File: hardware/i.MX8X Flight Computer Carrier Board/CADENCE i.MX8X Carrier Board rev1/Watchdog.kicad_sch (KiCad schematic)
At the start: 36 parts, among them U7 TLV1704

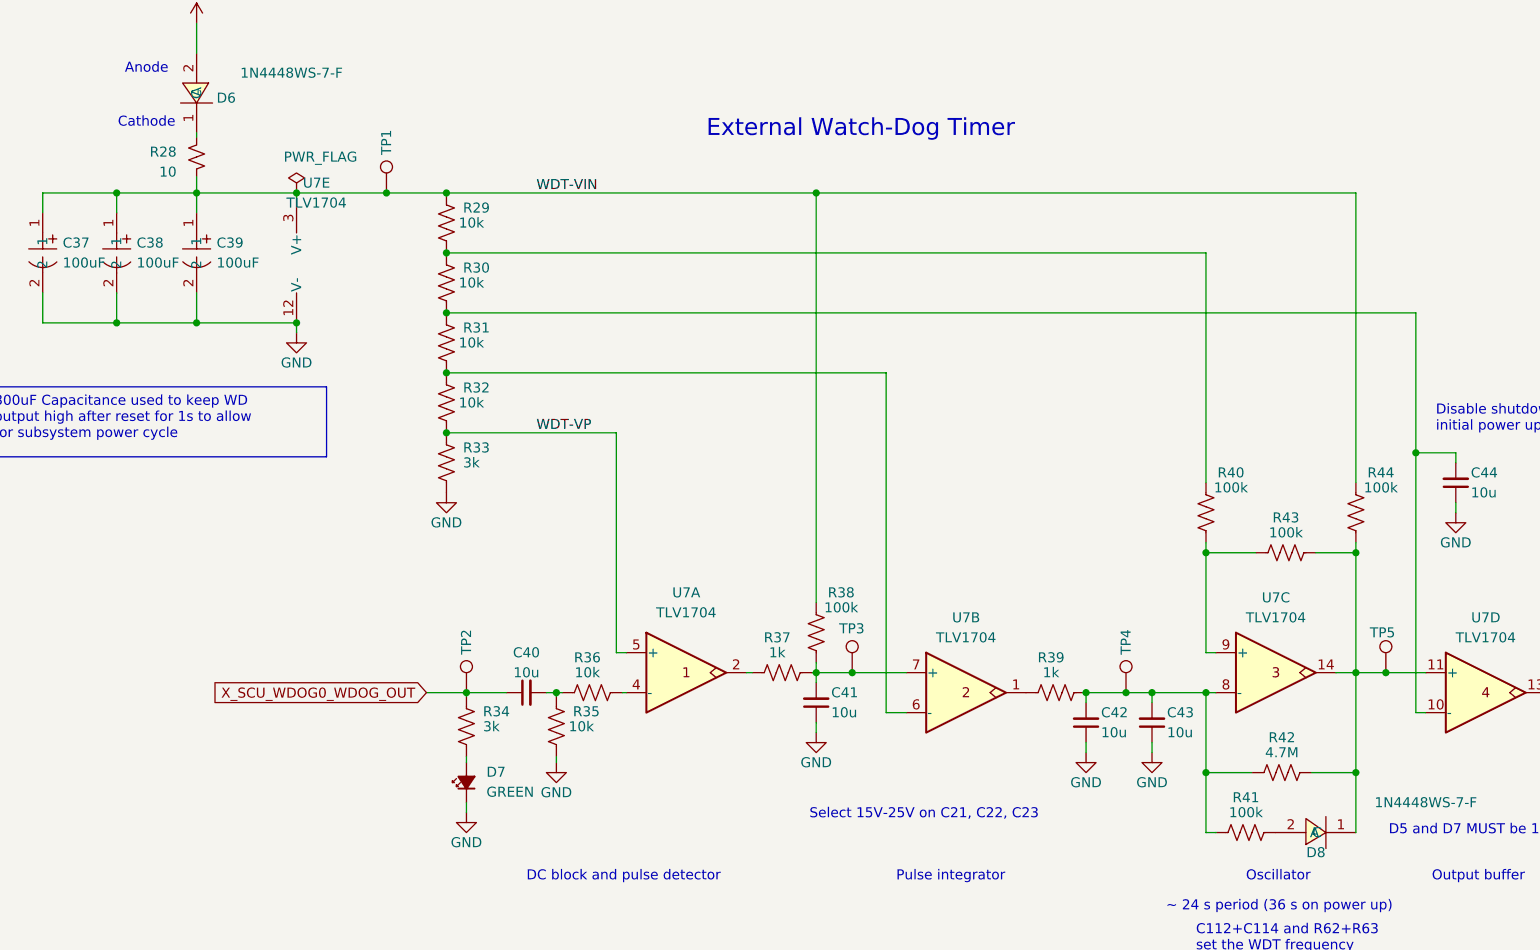
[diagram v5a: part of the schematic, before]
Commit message: Added pin definitions page
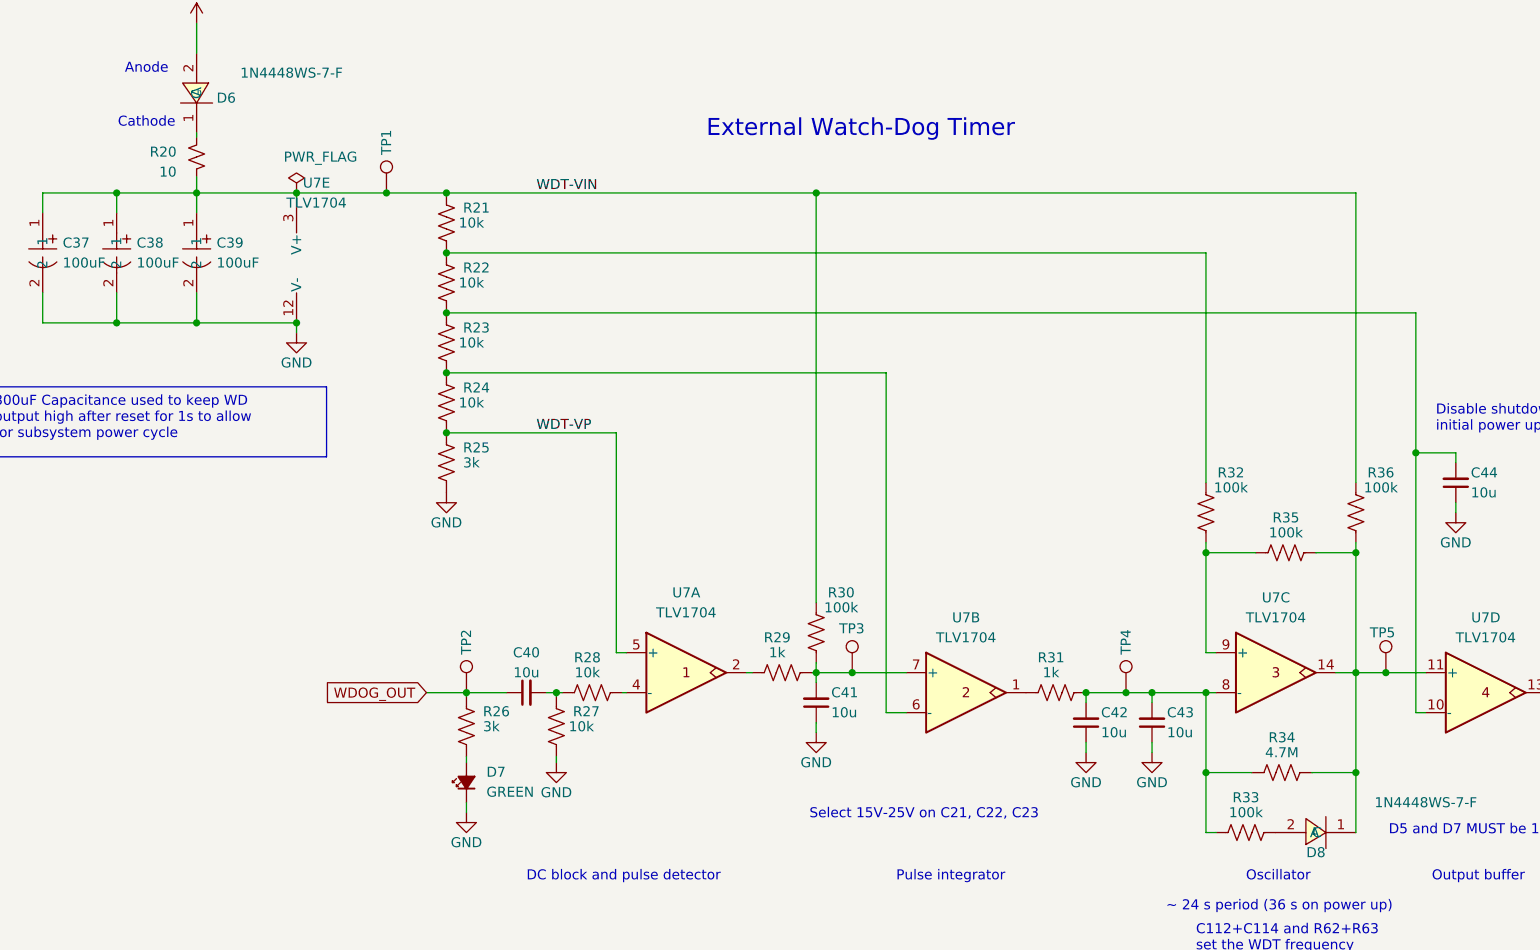
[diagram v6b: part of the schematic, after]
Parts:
- renumbered R28 to R20, R29 to R21, R30 to R22, R31 to R23, R32 to R24, R33 to R25, R34 to R26, R35 to R27, R36 to R28, R37 to R29, R38 to R30, R39 to R31, R40 to R32, R41 to R33, R42 to R34, R43 to R35, R44 to R36
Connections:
- net X_SCU_WDOG0_WDOG_OUT renamed WDOG_OUT
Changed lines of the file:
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@@
 		)
 	)
-	(global_label "X_SCU_WDOG0_WDOG_OUT"
+	(global_label "WDOG_OUT"
 		(shape input)
 		(at 77.47 114.3 180)
@@
 		)
 		(property "Intersheetrefs" "${INTERSHEET_REFS}"
-			(at 50.113 114.3 0)
+			(at 64.5667 114.3 0)
 			(effects
 				(font
@@
 		(on_board yes)
 		(dnp no)
-		(property "Reference" "R34"
+		(property "Reference" "R26"
 			(at 86.36 116.713 0)
 			(effects
@@
 			(project "CADENCE i.MX8X Carrier Board rev1"
 				(path "/de284495-d382-47cb-b528-76e440980d40/59642966-a844-41dc-8ff0-cc80b38f7a57"
-					(reference "R34")
+					(reference "R26")
 					(unit 1)
 				)
@@
 		(on_board yes)
 		(dnp no)
-		(property "Reference" "R36"
+		(property "Reference" "R28"
 			(at 97.917 109.855 90)
 			(effects
@@
 			(project "CADENCE i.MX8X Carrier Board rev1"
 				(path "/de284495-d382-47cb-b528-76e440980d40/59642966-a844-41dc-8ff0-cc80b38f7a57"
-					(reference "R36")
+					(reference "R28")
 					(unit 1)
 				)
@@
 		(on_board yes)
 		(dnp no)
-		(property "Reference" "R43"
+		(property "Reference" "R35"
 			(at 186.69 92.075 90)
 			(effects
@@
 			(project "CADENCE i.MX8X Carrier Board rev1"
 				(path "/de284495-d382-47cb-b528-76e440980d40/59642966-a844-41dc-8ff0-cc80b38f7a57"
-					(reference "R43")
+					(reference "R35")
 					(unit 1)
 				)
@@
 		(on_board yes)
 		(dnp no)
-		(property "Reference" "#PWR042"
+		(property "Reference" "#PWR043"
 			(at 93.98 129.54 0)
 			(effects
@@
 			(project "CADENCE i.MX8X Carrier Board rev1"
 				(path "/de284495-d382-47cb-b528-76e440980d40/59642966-a844-41dc-8ff0-cc80b38f7a57"
-					(reference "#PWR042")
+					(reference "#PWR043")
 					(unit 1)
 				)
@@
 		(on_board yes)
 		(dnp no)
-		(property "Reference" "#PWR041"
+		(property "Reference" "#PWR042"
 			(at 82.55 135.89 0)
 			(effects
@@
 			(project "CADENCE i.MX8X Carrier Board rev1"
 				(path "/de284495-d382-47cb-b528-76e440980d40/59642966-a844-41dc-8ff0-cc80b38f7a57"
-					(reference "#PWR041")
+					(reference "#PWR042")
 					(unit 1)
 				)
@@
 		(on_board yes)
 		(dnp no)
-		(property "Reference" "#PWR045"
+		(property "Reference" "#PWR046"
 			(at 169.672 128.27 0)
 			(effects
@@
 			(project "CADENCE i.MX8X Carrier Board rev1"
 				(path "/de284495-d382-47cb-b528-76e440980d40/59642966-a844-41dc-8ff0-cc80b38f7a57"
-					(reference "#PWR045")
+					(reference "#PWR046")
 					(unit 1)
 				)
@@
 		(on_board yes)
 		(dnp no)
-		(property "Reference" "#PWR040"
+		(property "Reference" "#PWR041"
 			(at 80.01 95.25 0)
 			(effects
@@
 			(project "CADENCE i.MX8X Carrier Board rev1"
 				(path "/de284495-d382-47cb-b528-76e440980d40/59642966-a844-41dc-8ff0-cc80b38f7a57"
-					(reference "#PWR040")
+					(reference "#PWR041")
 					(unit 1)
 				)
@@
 		(on_board yes)
 		(dnp no)
-		(property "Reference" "R30"
+		(property "Reference" "R22"
 			(at 83.82 60.325 0)
 			(effects
@@
 			(project "CADENCE i.MX8X Carrier Board rev1"
 				(path "/de284495-d382-47cb-b528-76e440980d40/59642966-a844-41dc-8ff0-cc80b38f7a57"
-					(reference "R30")
+					(reference "R22")
 					(unit 1)
 				)
@@
 		(on_board yes)
 		(dnp no)
-		(property "Reference" "R33"
+		(property "Reference" "R25"
 			(at 83.82 83.185 0)
 			(effects
@@
 			(project "CADENCE i.MX8X Carrier Board rev1"
 				(path "/de284495-d382-47cb-b528-76e440980d40/59642966-a844-41dc-8ff0-cc80b38f7a57"
-					(reference "R33")
+					(reference "R25")
 					(unit 1)
 				)
@@
 		(on_board yes)
 		(dnp no)
-		(property "Reference" "R39"
+		(property "Reference" "R31"
 			(at 156.845 109.855 90)
 			(effects
@@
 			(project "CADENCE i.MX8X Carrier Board rev1"
 				(path "/de284495-d382-47cb-b528-76e440980d40/59642966-a844-41dc-8ff0-cc80b38f7a57"
-					(reference "R39")
+					(reference "R31")
 					(unit 1)
 				)
@@
 		(on_board yes)
 		(dnp no)
-		(property "Reference" "R31"
+		(property "Reference" "R23"
 			(at 83.82 67.945 0)
 			(effects
@@
 			(project "CADENCE i.MX8X Carrier Board rev1"
 				(path "/de284495-d382-47cb-b528-76e440980d40/59642966-a844-41dc-8ff0-cc80b38f7a57"
-					(reference "R31")
+					(reference "R23")
 					(unit 1)
 				)
@@
 		(on_board yes)
 		(dnp no)
-		(property "Reference" "#PWR043"
+		(property "Reference" "#PWR044"
 			(at 127 125.73 0)
 			(effects
@@
 			(project "CADENCE i.MX8X Carrier Board rev1"
 				(path "/de284495-d382-47cb-b528-76e440980d40/59642966-a844-41dc-8ff0-cc80b38f7a57"
-					(reference "#PWR043")
+					(reference "#PWR044")
 					(unit 1)
 				)
@@
 		(on_board yes)
 		(dnp no)
-		(property "Reference" "R32"
+		(property "Reference" "R24"
 			(at 83.82 75.565 0)
 			(effects
@@
 			(project "CADENCE i.MX8X Carrier Board rev1"
 				(path "/de284495-d382-47cb-b528-76e440980d40/59642966-a844-41dc-8ff0-cc80b38f7a57"
-					(reference "R32")
+					(reference "R24")
 					(unit 1)
 				)
@@
 		(on_board yes)
 		(dnp no)
-		(property "Reference" "#PWR039"
+		(property "Reference" "#PWR040"
 			(at 60.96 74.93 0)
 			(effects
@@
 			(project "CADENCE i.MX8X Carrier Board rev1"
 				(path "/de284495-d382-47cb-b528-76e440980d40/59642966-a844-41dc-8ff0-cc80b38f7a57"
-					(reference "#PWR039")
+					(reference "#PWR040")
 					(unit 1)
 				)
@@
 		(on_board yes)
 		(dnp no)
-		(property "Reference" "#PWR044"
+		(property "Reference" "#PWR045"
 			(at 161.29 128.27 0)
 			(effects
@@
 			(project "CADENCE i.MX8X Carrier Board rev1"
 				(path "/de284495-d382-47cb-b528-76e440980d40/59642966-a844-41dc-8ff0-cc80b38f7a57"
-					(reference "#PWR044")
+					(reference "#PWR045")
 					(unit 1)
 				)
@@
 		(on_board yes)
 		(dnp no)
-		(property "Reference" "R28"
+		(property "Reference" "R20"
 			(at 45.72 45.593 0)
 			(effects
@@
 			(project "CADENCE i.MX8X Carrier Board rev1"
 				(path "/de284495-d382-47cb-b528-76e440980d40/59642966-a844-41dc-8ff0-cc80b38f7a57"
-					(reference "R28")
+					(reference "R20")
 					(unit 1)
 				)
@@
 		(on_board yes)
 		(dnp no)
-		(property "Reference" "R44"
+		(property "Reference" "R36"
 			(at 198.755 86.36 0)
 			(effects
@@
 			(project "CADENCE i.MX8X Carrier Board rev1"
 				(path "/de284495-d382-47cb-b528-76e440980d40/59642966-a844-41dc-8ff0-cc80b38f7a57"
-					(reference "R44")
+					(reference "R36")
 					(unit 1)
 				)
@@
 		(on_board yes)
 		(dnp no)
-		(property "Reference" "R37"
+		(property "Reference" "R29"
 			(at 122.047 107.315 90)
 			(effects
@@
 			(project "CADENCE i.MX8X Carrier Board rev1"
 				(path "/de284495-d382-47cb-b528-76e440980d40/59642966-a844-41dc-8ff0-cc80b38f7a57"
-					(reference "R37")
+					(reference "R29")
 					(unit 1)
 				)
@@
 		(on_board yes)
 		(dnp no)
-		(property "Reference" "R41"
+		(property "Reference" "R33"
 			(at 181.61 127.635 90)
 			(effects
@@
 			(project "CADENCE i.MX8X Carrier Board rev1"
 				(path "/de284495-d382-47cb-b528-76e440980d40/59642966-a844-41dc-8ff0-cc80b38f7a57"
-					(reference "R41")
+					(reference "R33")
 					(unit 1)
 				)
@@
 		(dnp no)
 		(fields_autoplaced yes)
-		(property "Reference" "#PWR038"
+		(property "Reference" "#PWR039"
 			(at 48.26 33.02 0)
 			(effects
@@
 			(project "CADENCE i.MX8X Carrier Board rev1"
 				(path "/de284495-d382-47cb-b528-76e440980d40/59642966-a844-41dc-8ff0-cc80b38f7a57"
-					(reference "#PWR038")
+					(reference "#PWR039")
 					(unit 1)
 				)
@@
 		(on_board yes)
 		(dnp no)
-		(property "Reference" "R38"
+		(property "Reference" "R30"
 			(at 130.175 101.6 0)
 			(effects
@@
 			(project "CADENCE i.MX8X Carrier Board rev1"
 				(path "/de284495-d382-47cb-b528-76e440980d40/59642966-a844-41dc-8ff0-cc80b38f7a57"
-					(reference "R38")
+					(reference "R30")
 					(unit 1)
 				)
@@
 		(on_board yes)
 		(dnp no)
-		(property "Reference" "#PWR046"
+		(property "Reference" "#PWR047"
 			(at 208.28 97.79 0)
 			(effects
@@
 			(project "CADENCE i.MX8X Carrier Board rev1"
 				(path "/de284495-d382-47cb-b528-76e440980d40/59642966-a844-41dc-8ff0-cc80b38f7a57"
-					(reference "#PWR046")
+					(reference "#PWR047")
 					(unit 1)
 				)
@@
 		(on_board yes)
 		(dnp no)
-		(property "Reference" "R35"
+		(property "Reference" "R27"
 			(at 97.79 116.713 0)
 			(effects
@@
 			(project "CADENCE i.MX8X Carrier Board rev1"
 				(path "/de284495-d382-47cb-b528-76e440980d40/59642966-a844-41dc-8ff0-cc80b38f7a57"
-					(reference "R35")
+					(reference "R27")
 					(unit 1)
 				)
@@
 		(on_board yes)
 		(dnp no)
-		(property "Reference" "R42"
+		(property "Reference" "R34"
 			(at 186.182 120.015 90)
 			(effects
@@
 			(project "CADENCE i.MX8X Carrier Board rev1"
 				(path "/de284495-d382-47cb-b528-76e440980d40/59642966-a844-41dc-8ff0-cc80b38f7a57"
-					(reference "R42")
+					(reference "R34")
 					(unit 1)
 				)
@@
 		(on_board yes)
 		(dnp no)
-		(property "Reference" "R29"
+		(property "Reference" "R21"
 			(at 83.82 52.705 0)
 			(effects
@@
 			(project "CADENCE i.MX8X Carrier Board rev1"
 				(path "/de284495-d382-47cb-b528-76e440980d40/59642966-a844-41dc-8ff0-cc80b38f7a57"
-					(reference "R29")
+					(reference "R21")
 					(unit 1)
 				)
@@
 		(on_board yes)
 		(dnp no)
-		(property "Reference" "R40"
+		(property "Reference" "R32"
 			(at 179.705 86.36 0)
 			(effects
@@
 			(project "CADENCE i.MX8X Carrier Board rev1"
 				(path "/de284495-d382-47cb-b528-76e440980d40/59642966-a844-41dc-8ff0-cc80b38f7a57"
-					(reference "R40")
+					(reference "R32")
 					(unit 1)
 				)

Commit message: oops the real push here
previous push description/title describes this content push
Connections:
- net WDOG_OUT renamed X_JTAG_TRST (WDOG_OUT)
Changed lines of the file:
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@@
-		)
-	)
-	(global_label "WDOG_OUT"
-		(shape input)
-		(at 77.47 114.3 180)
-		(fields_autoplaced yes)
-		(effects
-			(font
-				(size 1.27 1.27)
-			)
-			(justify right)
-		)
-		(property "Intersheetrefs" "${INTERSHEET_REFS}"
-			(at 64.5667 114.3 0)
-			(effects
-				(font
-					(size 1.27 1.27)
-				)
-				(justify right)
-				(hide yes)
-			)
 		)
 	)
@@
 			(effects
 				(font
+					(size 1.27 1.27)
+				)
+				(hide yes)
+			)
+		)
+	)
+	(global_label "X_JTAG_TRST (WDOG_OUT)"
+		(shape input)
+		(at 77.47 114.3 180)
+		(effects
+			(font
+				(size 1.27 1.27)
+			)
+			(justify right)
+		)
+		(property "Intersheetrefs" "${INTERSHEET_REFS}"
+			(at 77.47 114.3 0)
+			(effects
+				(font
